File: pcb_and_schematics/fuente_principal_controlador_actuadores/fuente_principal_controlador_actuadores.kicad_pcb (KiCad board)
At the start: 2 copper layers, 78 parts, among them J1 Screw_Terminal_01x02, J10 Screw_Terminal_01x02, J11 Conn_01x15_Female, J12 Conn_01x15_Female, J2 Screw_Terminal_01x02, J3 Screw_Terminal_01x02, J4 Screw_Terminal_01x02, J5 Screw_Terminal_01x02, J6 Screw_Terminal_01x02, J7 Screw_Terminal_01x02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

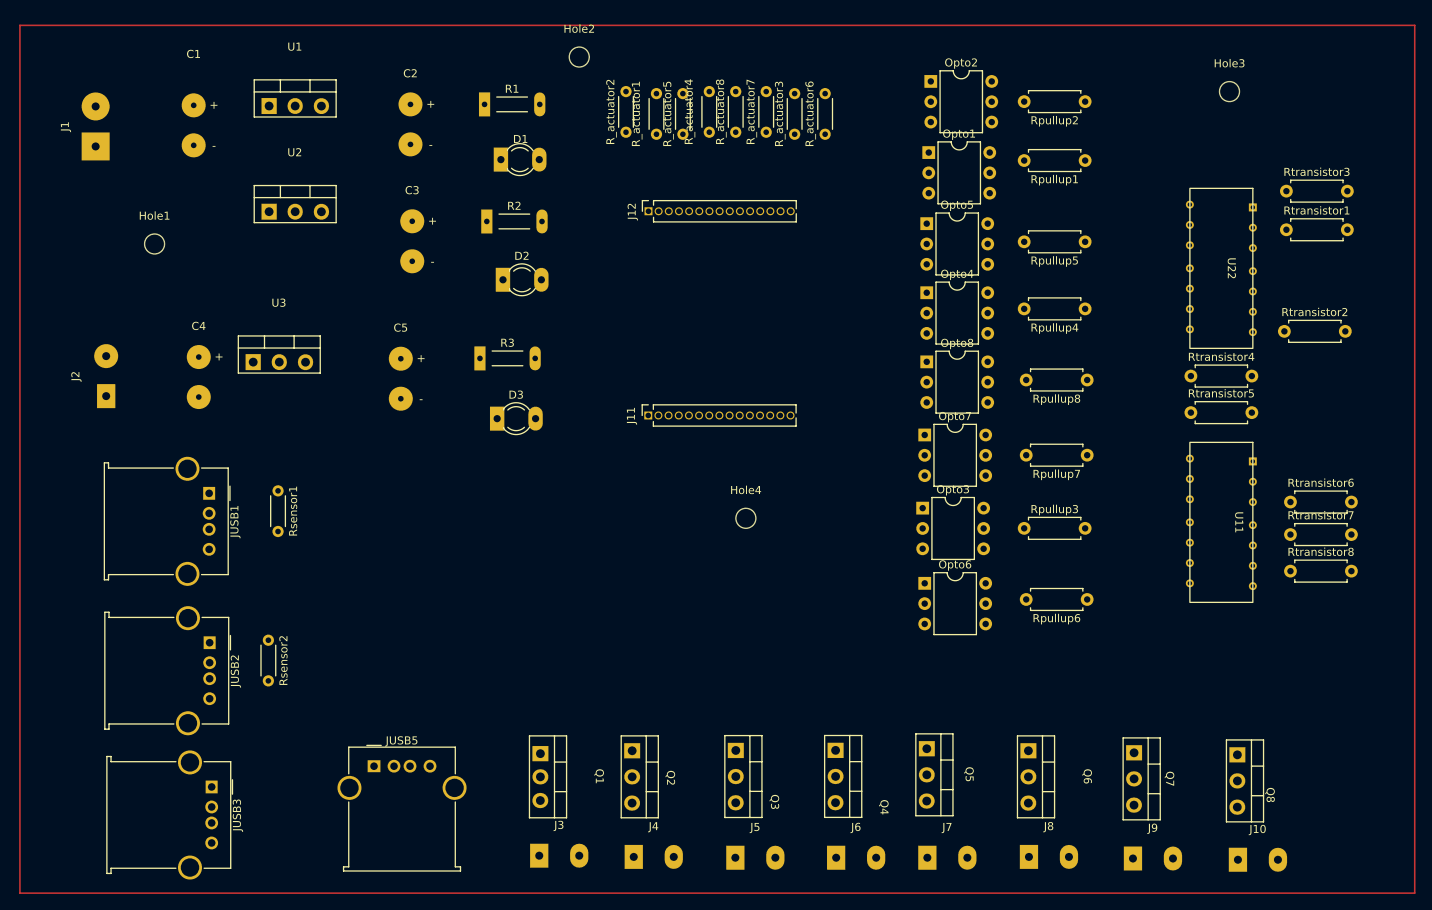
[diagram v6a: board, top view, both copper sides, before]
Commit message: reestructuration of pin connections in the schematic, addition of shared ground lines, and recrease in anchor by 1 cm
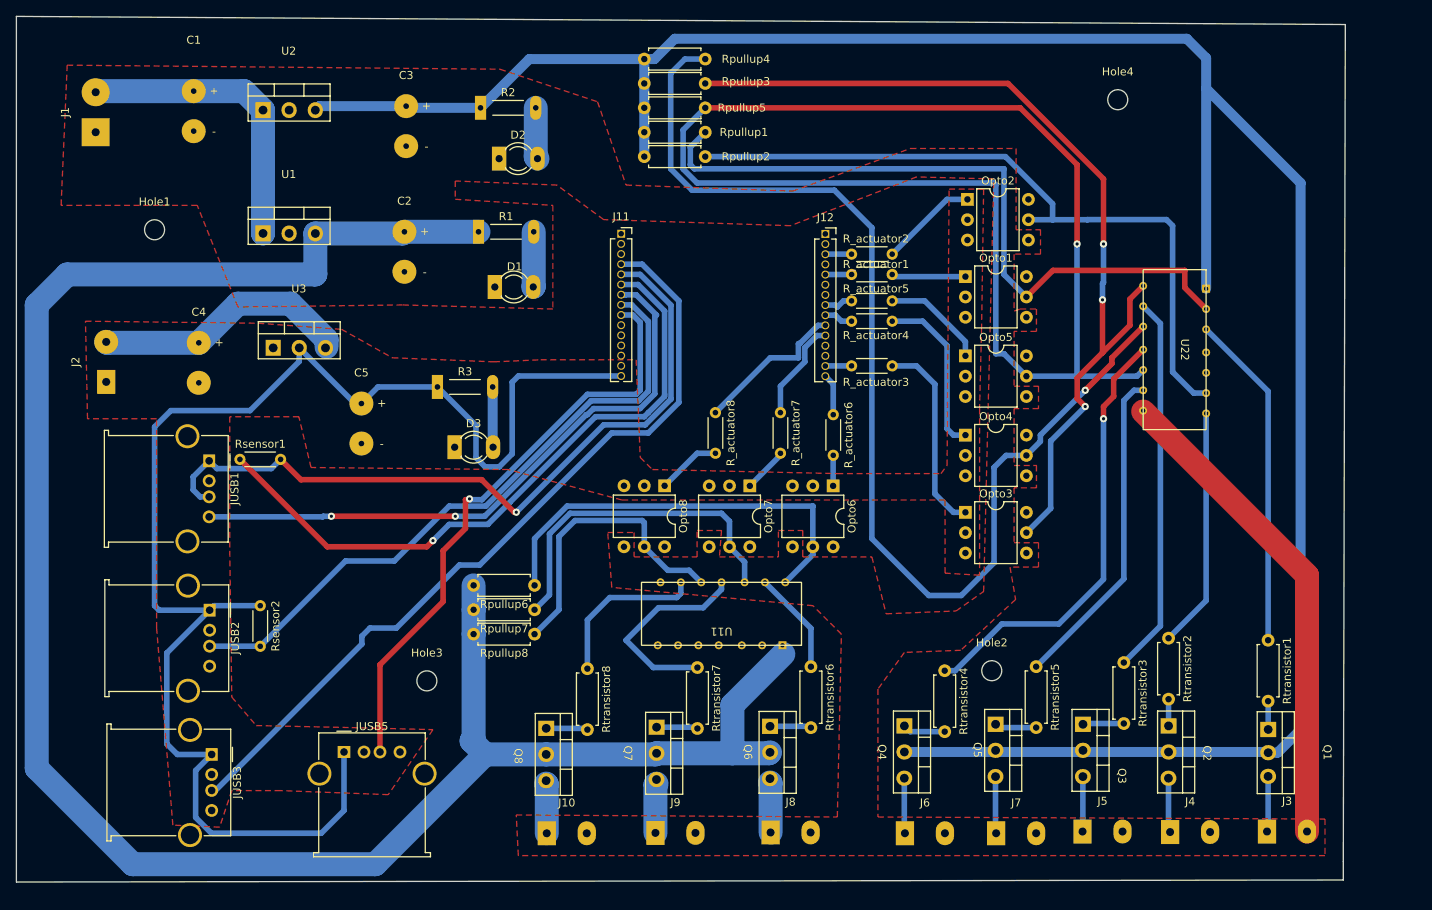
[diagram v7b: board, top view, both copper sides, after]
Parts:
- moved Hole3 124.5 mm to (86.1, 107.2)
- moved Hole2 92.4 mm to (156.7, 105.9)
- moved J3 91.0 mm to (193.6, 126.0)
- moved Q1 91.0 mm to (192.1, 116.1)
- moved Rtransistor8 88.7 mm to (106.2, 105.7), turned to -90 degrees
- moved J10 86.5 mm to (103.6, 126.2)
- moved Q8 86.5 mm to (101.8, 116.3)
- moved Rpullup8 76.0 mm to (99.6, 101.3)
- moved Rtransistor7 76.0 mm to (119.9, 105.5), turned to -90 degrees
- moved Rpullup7 71.7 mm to (99.6, 98.3)
- moved Hole4 70.0 mm to (172.5, 34.5)
- moved Rpullup6 69.1 mm to (99.6, 95.2)
- moved Rpullup3 68.4 mm to (120.9, 32.5), turned to 180 degrees
- moved J4 67.1 mm to (181.5, 126.1)
- moved Q2 67.1 mm to (179.6, 116.0)
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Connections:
- Opto3 pad 2: 3.3V DC esp32 -> GND 3.3V
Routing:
- net 5.0VDC pot: track 0.00 -> 293.0 mm
- net 12.0VDC pot: track 0.00 -> 259.3 mm
- net 3.3VDC: track 0.00 -> 181.7 mm
- net Net-(Opto5-Pad5): track 0.00 -> 165.6 mm, vias 0 -> 1
- net Net-(Opto4-Pad5): track 0.00 -> 142.7 mm, vias 0 -> 1
- net Net-(Opto3-Pad5): track 0.00 -> 114.2 mm, vias 0 -> 3
- net signal PH: track 0.00 -> 100.9 mm
- net signal EC: track 0.00 -> 93.6 mm, vias 0 -> 1
- net Net-(Opto2-Pad5): track 0.00 -> 89.8 mm
- net Net-(Opto1-Pad5): track 0.00 -> 88.5 mm
- net 3.3V ec: track 0.00 -> 82.9 mm, vias 0 -> 1
- net signal DB18B20: track 0.00 -> 81.0 mm
- net GND ec: track 0.00 -> 77.5 mm, vias 0 -> 2
- net Signal ExtraSensor: track 0.00 -> 74.7 mm, vias 0 -> 1
- net GND pot: track 0.00 -> 61.0 mm
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- added copper zone on F.Cu, net GND 3.3V
- added copper zone on F.Cu, net GND pot
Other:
- board outline added: 166.1 x 108.2 mm
